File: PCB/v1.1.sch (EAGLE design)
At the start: 48 parts, among them IC1 MEGA8-P

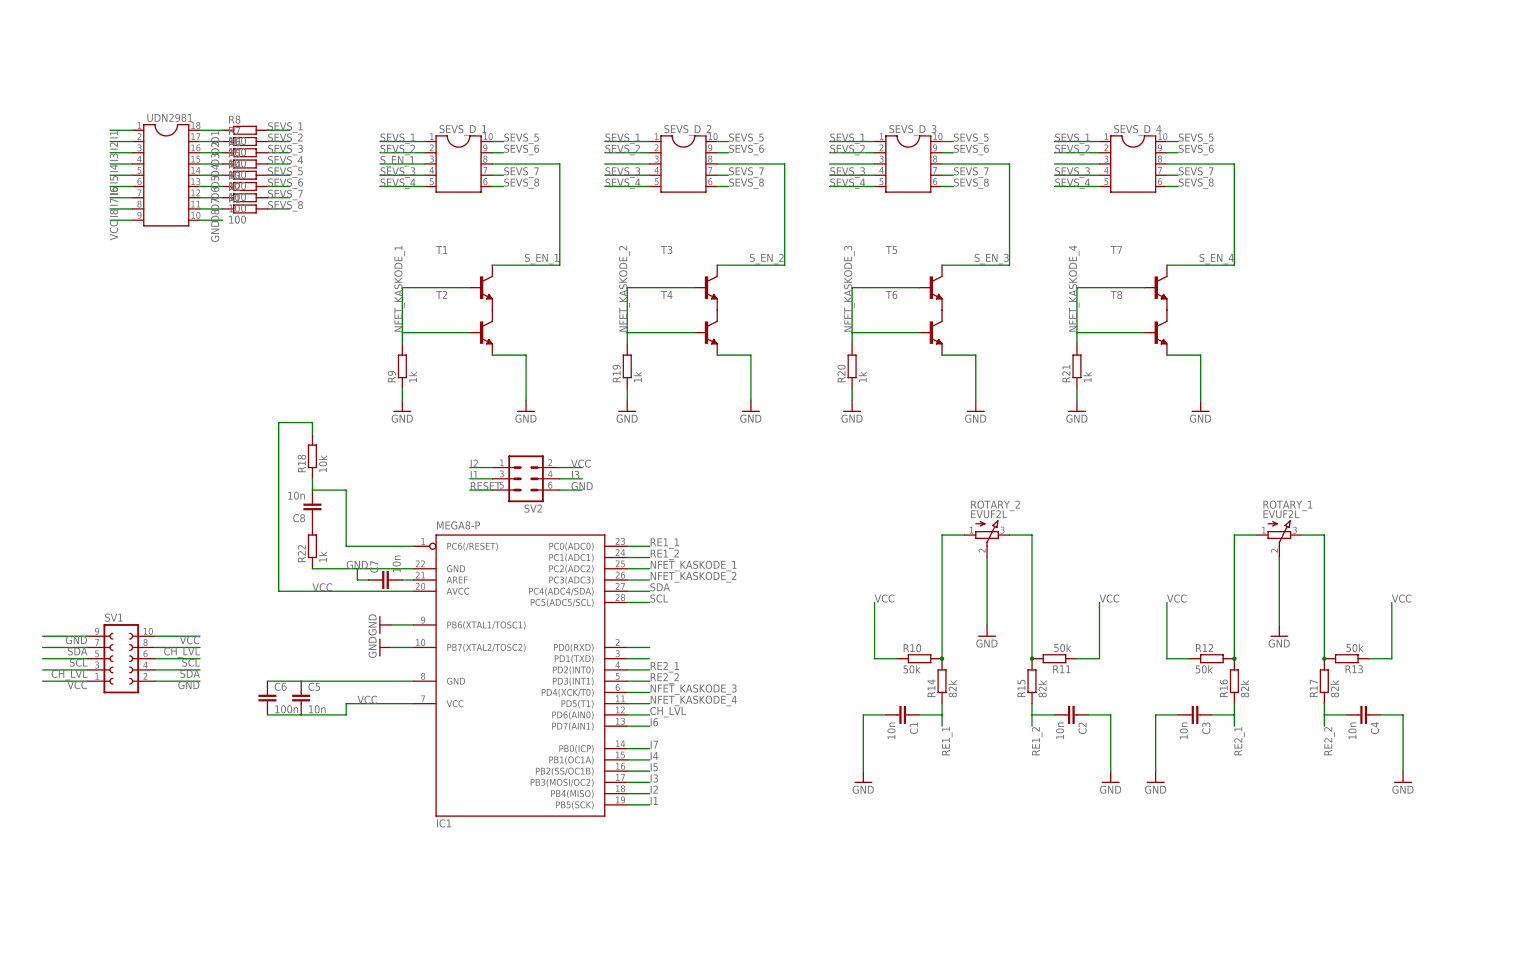
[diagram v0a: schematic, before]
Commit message: Tidying up
Some useful order in schematic
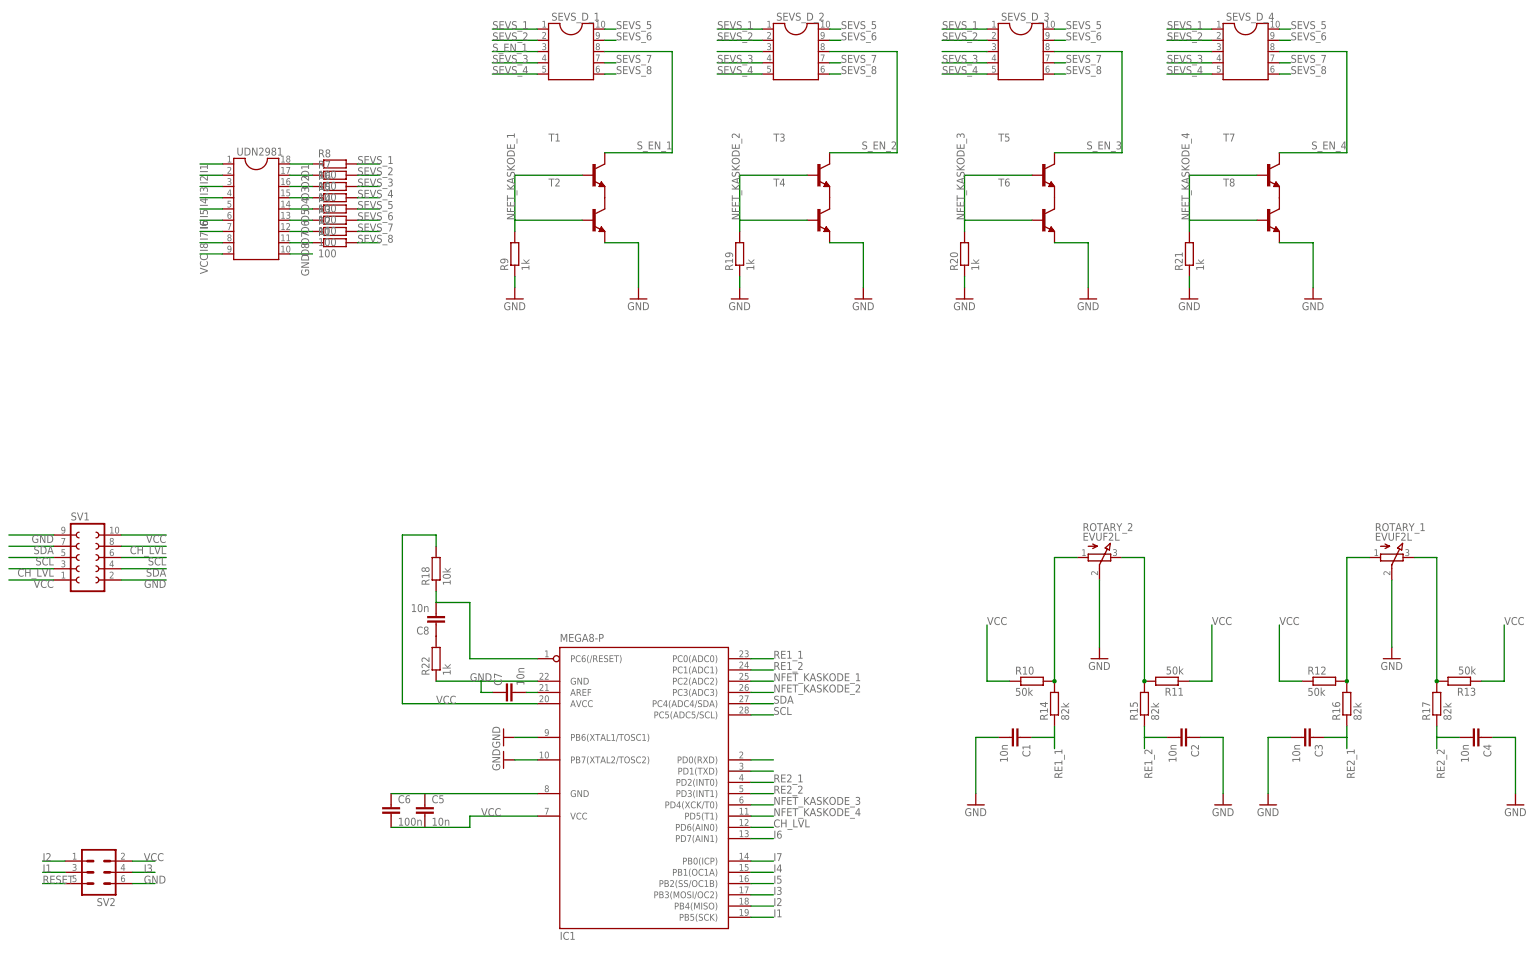
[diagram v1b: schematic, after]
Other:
- note added: "Designer: Florian Heptner Projekt: 4x7segment output, 2xRotary Enc input"
- note added: "I2C to outside world"
- note added: "Rotary Encoders"
- note added: "Seven Segments + Driving"
- note added: "microcontroller"
- note added: "programming adapter"
- moved on the sheet: C1, C2, C3, C4, C5, C6, C7, C8, IC1, R1, R10, R11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
